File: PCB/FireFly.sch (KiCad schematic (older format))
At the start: 86 parts, among them Q1 LED_RGB 5050, Q2 MMBT2222, SW4 SWITCH

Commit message: Sch seems done
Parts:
- removed C2, C3: 0.1u, Capacitors:CAP_0603, symbol Tittar_kl:C
- removed C6: 1u, Capacitors:CAP_0603, symbol Tittar_kl:C
- removed C9: 10u, Capacitors:CAP_0603, symbol Tittar_kl:C
- removed L2: BLM15AG102SN1, Inductors:IND_0402, symbol Tittar_kl:L
- added C15: 100pF, Capacitors:CAP_0402, symbol Tittar_kl:C
- added C34: *, Capacitors:CAP_0402, symbol Tittar_kl:C
- added SW1, SW3: BUTTON, symbol Switches:BUTTON
- added XL2: CONN_5, symbol Connectors_kl:CONN_5
- C33: renamed from C23; value 3.3pF -> *
- C4: value 0.1u -> 12pF; footprint Capacitors:CAP_0603 -> Capacitors:CAP_0402; Price (none) -> 0.5; SolderPoints (none) -> 2
- C5: value 10n -> 12pF; footprint Capacitors:CAP_0603 -> Capacitors:CAP_0402; Price (none) -> 0.5; SolderPoints (none) -> 2
- L8: renamed from L4; value 8.2nH -> *
- gave numbers to parts that had none: 27
- renumbered ANT1 to ANT2, C10 to C18, C7 to C2, C11 to C22, C12 to C23, C13 to C24, C22 to C25, C14 to C26, C15 to C27, C16 to C28, C17 to C29, C18 to C30, C19 to C31, C26 to C32, C8 to C6, L3 to L7, R9 to R10, R12 to R11, R8 to R12, R1 to R2, R2 to R3, R3 to R4, R4 to R5, R5 to R7, R6 to R8, R7 to R9, SW4 to SW2, TP2 to TP1, TP3 to TP2, XL2 to XL3, XTAL1 to XTAL3
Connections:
- net labels added: P27, P28, P29
- net labels removed: ANT1, ANT2, BTN3, DIP1, DIP2, DIP3, DIP4, DIP5, DIP6, DIP7, DIP8, MCU_RX_NRF_TX, MCU_TX_NRF_RX, PwrMCU, SWCLK, SWDIO, UART_RX, UART_TX, Vibro_CTRL
- wire segments 327 -> 308
- no-connect marks 9 -> 4
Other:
- note added: "Just pins"
- note removed: "MCU Power Filter"
- note removed: "Pins 24, 36, 48, 1+9"
- moved on the sheet: ANT1, ANT2, B1, BLN1, BZ1, C1, C10, C11, C12, C13, C14, C16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

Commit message: pcb under construction
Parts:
- ANT1: footprint (none) -> Antennas:LcktSnd_868
- ANT2: footprint Antennas:Locket5 -> Antennas:LcktSnd_2d41
- DD1: footprint (none) -> SO_DIL_TSSOP:SO8_150MIL
- SW1, SW3: footprint (none) -> BtnsSwitches:BTN_4x4_SMD
- XL1: footprint (none) -> Connectors:PLD-8
- XL2: footprint (none) -> Connectors:PLS-5
- XTAL2: footprint CRYSTAL -> Quartz:03225C4
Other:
- moved on the sheet: Logo1
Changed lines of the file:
@@
 L pcb_details:Logo Logo1
 U 1 1 57188192
-P 14700 9150
-F 0 "Logo1" H 14600 9600 60  0000 C CNN
-F 1 "Logo" H 14900 9600 60  0000 C CNN
-F 2 "Pictures:Ostranna_12d7_10d1" H 14700 9150 60  0001 C CNN
-F 3 "" H 14700 9150 60  0000 C CNN
-	1    14700 9150
+P 15200 9150
+F 0 "Logo1" H 15100 9600 60  0000 C CNN
+F 1 "Logo" H 15400 9600 60  0000 C CNN
+F 2 "Pictures:Ostranna_12d7_10d1" H 15200 9150 60  0001 C CNN
+F 3 "" H 15200 9150 60  0000 C CNN
+	1    15200 9150
 	1    0    0    -1
 $EndComp
@@
 F 0 "XTAL2" V 6200 2650 50  0000 L CNN
 F 1 "32MHz" V 5950 2600 50  0000 L CNN
-F 2 "CRYSTAL" H 6125 3025 39  0001 C CNN
+F 2 "Quartz:03225C4" H 6125 3025 39  0001 C CNN
 F 3 "" H 6100 3175 60  0001 C CNN
 F 4 "15" H 6200 3275 60  0001 C CNN "Price"
@@
 F 0 "ANT1" H 8267 1647 60  0000 C CNN
 F 1 "ANT_GENERAL" H 8267 1541 60  0000 C CNN
-F 2 "" H 8400 1350 60  0000 C CNN
+F 2 "Antennas:LcktSnd_868" H 8400 1350 60  0001 C CNN
 F 3 "" H 8400 1350 60  0000 C CNN
 	1    8400 1350
@@
 F 0 "DD1" H 1450 4637 60  0000 C CNN
 F 1 "EEPROM_I2C" H 1450 4531 60  0000 C CNN
-F 2 "" H 2000 4400 60  0001 C CNN
+F 2 "SO_DIL_TSSOP:SO8_150MIL" H 2000 4400 60  0001 C CNN
 F 3 "" H 1900 4500 60  0001 C CNN
 F 4 "8" H 1600 4700 60  0001 C CNN "SolderPoints"
@@
 F 0 "XL1" H 842 2036 50  0000 C CNN
 F 1 "CONN_8" H 842 1945 50  0000 C CNN
-F 2 "" H 900 1450 60  0000 C CNN
+F 2 "Connectors:PLD-8" H 900 1450 60  0001 C CNN
 F 3 "" H 900 1450 60  0000 C CNN
 	1    900  1450
@@
 F 0 "ANT2" H 15150 1550 60  0000 C CNN
 F 1 "ANT_PCB_MONO_2PIN" H 15400 1550 60  0001 C CNN
-F 2 "Antennas:Locket5" H 15050 1400 60  0001 C CNN
+F 2 "Antennas:LcktSnd_2d41" H 15050 1400 60  0001 C CNN
 F 3 "" H 15050 1400 60  0000 C CNN
 F 4 "0" H 15050 1400 60  0001 C CNN "Price"
@@
 F 0 "SW1" H 6150 8605 50  0000 C CNN
 F 1 "BUTTON" H 6150 8514 50  0000 C CNN
-F 2 "" H 6150 8350 60  0000 C CNN
+F 2 "BtnsSwitches:BTN_4x4_SMD" H 6150 8350 60  0001 C CNN
 F 3 "" H 6150 8350 60  0000 C CNN
 	1    6150 8350
@@
 F 0 "SW3" H 7650 8605 50  0000 C CNN
 F 1 "BUTTON" H 7650 8514 50  0000 C CNN
-F 2 "" H 7650 8350 60  0000 C CNN
+F 2 "BtnsSwitches:BTN_4x4_SMD" H 7650 8350 60  0001 C CNN
 F 3 "" H 7650 8350 60  0000 C CNN
 	1    7650 8350
@@
 F 0 "XL2" H 842 3186 50  0000 C CNN
 F 1 "CONN_5" H 842 3095 50  0000 C CNN
-F 2 "" H 900 2750 60  0000 C CNN
+F 2 "Connectors:PLS-5" H 900 2750 60  0001 C CNN
 F 3 "" H 900 2750 60  0000 C CNN
 	1    900  2750

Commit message: v1 sent to factory
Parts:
- removed C15, C32: 100pF, Capacitors:CAP_0402, symbol Tittar_kl:C
- removed C16, C20: *, Capacitors:CAP_0402, symbol Tittar_kl:C
- removed L5: *, Inductors:IND_0402, symbol Tittar_kl:L
- removed RP3, RP4: REFPOINT, PCB:REF_POINT_1MM, symbol pcb_details:REFPOINT
- removed XL2: CONN_5, Connectors:PLS-5, symbol Connectors_kl:CONN_5
- added XL2: CONN_4, Connectors:PLS-4, symbol Connectors_kl:CONN_4
- ANT1: footprint Antennas:LcktSnd_868 -> Antennas:Firefly_2400; symbol Antennas_kl:ANT_GENERAL -> Antennas_kl:ANT_PCB_MONO
- ANT2: footprint Antennas:LcktSnd_2d41 -> Antennas:Firefly_868; symbol Antennas_kl:ANT_PCB_MONO_2PIN -> Antennas_kl:ANT_PCB_MONO
- C14, C17, C2, C21, C22, C23, C24, C26, C27, C28, C29, C3, C30, C31, C9: footprint Capacitors:CAP_0603 -> Capacitors:CAP_0402
- XL1: footprint Connectors:PLD-8 -> Connectors:PLD-8_LOCK
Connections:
- net P29 is gone; now on net VDD_NRF: DD2.41 (P0.29/AIN5)
- net +BATT: now also XL2.2 (PM)
- net GND: now also XL2.1 (P1); no longer ANT1.2 (GND), ANT2.2
- net NRF_NRST: now also XL1.8; no longer XL1.7
- net NRF_SWCLK: now also XL1.4; no longer XL1.2
- net NRF_SWDIO: now also XL1.2; no longer XL1.4
- net NRF_SWO: now also XL1.7; no longer XL1.8
- net P27: now also XL2.3
- net P28: now also XL2.4
- net RF3: now also C33.1, L8.2
- net RF2400: now reaches ANT1.1
- net RF2400: now also L3.2
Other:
- note added: "Battery\nmeasurement"
- moved on the sheet: C33, C34, L8

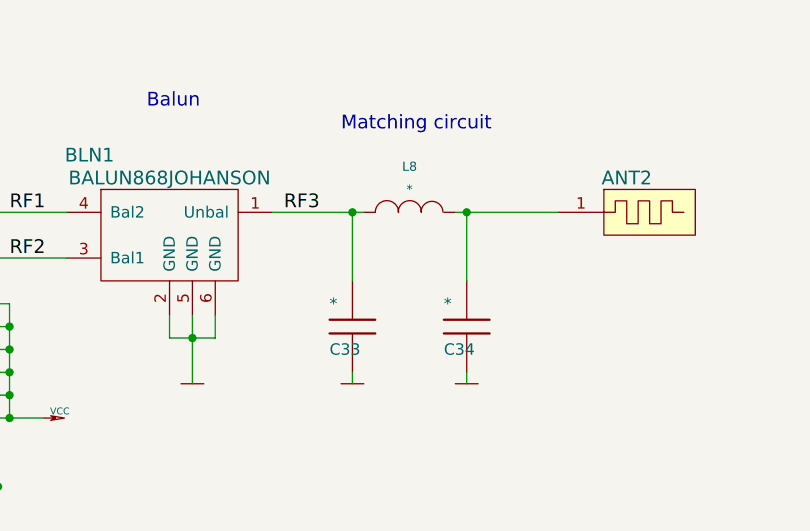
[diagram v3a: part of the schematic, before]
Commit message: Antenna matched
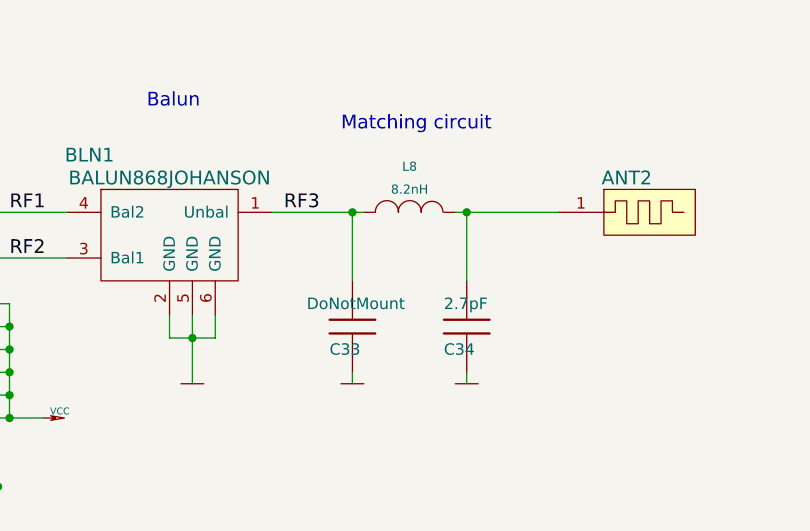
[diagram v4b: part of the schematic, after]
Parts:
- C33: value * -> DoNotMount
- C34: value * -> 2.7pF
- L8: value * -> 8.2nH
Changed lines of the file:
@@
 EESchema Schematic File Version 5
 LIBS:FireFly-cache
-EELAYER 29 0
+EELAYER 30 0
 EELAYER END
 $Descr A3 16535 11693
@@
 Comment3 ""
 Comment4 ""
+Comment5 ""
+Comment6 ""
+Comment7 ""
+Comment8 ""
+Comment9 ""
 $EndDescr
 $Comp
@@
 P 13550 1850
 F 0 "C33" H 13450 1750 50  0000 L CNN
-F 1 "*" H 13450 1950 50  0000 L CNN
+F 1 "DoNotMount" H 13350 1950 50  0000 L CNN
 F 2 "Capacitors:CAP_0402" V 13650 1700 28  0001 C BNN
 F 3 "" H 13450 1750 60  0001 C CNN
@@
 P 14050 1850
 F 0 "C34" H 13950 1750 50  0000 L CNN
-F 1 "*" H 13950 1950 50  0000 L CNN
+F 1 "2.7pF" H 13950 1950 50  0000 L CNN
 F 2 "Capacitors:CAP_0402" V 14150 1700 28  0001 C BNN
 F 3 "" H 13950 1750 60  0001 C CNN
@@
 P 13800 1350
 F 0 "L8" V 14000 1350 40  0000 C CNN
-F 1 "*" V 13900 1350 40  0000 C CNN
+F 1 "8.2nH" V 13900 1350 40  0000 C CNN
 F 2 "Inductors:IND_0402" V 13860 1360 40  0001 C CNN
 F 3 "" V 13700 1210 60  0001 C CNN

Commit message: Preparing for production
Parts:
- added D2: BAT54WS, Diodes:SOD323, symbol Tittar_kl:D_Shottky
- B1: footprint Installation:BATTERY_AAA_X2 -> Installation:BATTERY_AAA_X2_PLUS_LEFT
- BZ1: value PS-9627 -> KLJ-09650-3027; footprint Installation:BUZZER_HC0903 -> Installation:BUZZER_KLJ-09650-3027; Price 10 -> (none); URL http://www.quartz1.com/price/model.php?akt=7940.06 -> (none)
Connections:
- net +BATT: now also D2.C
- net BuzzerOut: now also D2.A
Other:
- moved on the sheet: BZ1
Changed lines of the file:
@@
 EESchema Schematic File Version 5
-LIBS:FireFly-cache
 EELAYER 30 0
 EELAYER END
@@
 $EndComp
 Wire Wire Line
-	7700 6250 7950 6250
+	7800 6250 7850 6250
 Wire Wire Line
 	5200 6450 5650 6450
@@
 	6150 6450 6250 6450
 Wire Wire Line
-	6500 6250 7200 6250
+	6500 6250 7250 6250
 $Comp
 L Transistors_kl:NPN Q2
@@
 L power:+BATT #PWR042
 U 1 1 572478CD
-P 7950 6250
-F 0 "#PWR042" H 7950 6210 30  0001 C CNN
-F 1 "+BATT" H 8030 6280 30  0000 C CNN
-F 2 "" H 7950 6250 60  0000 C CNN
-F 3 "" H 7950 6250 60  0000 C CNN
-	1    7950 6250
+P 8050 6250
+F 0 "#PWR042" H 8050 6210 30  0001 C CNN
+F 1 "+BATT" H 8130 6280 30  0000 C CNN
+F 2 "" H 8050 6250 60  0000 C CNN
+F 3 "" H 8050 6250 60  0000 C CNN
+	1    8050 6250
 	1    0    0    -1
 $EndComp
@@
 L Tittar_kl:BUZZER BZ1
 U 1 1 57C421AE
-P 7450 6250
-F 0 "BZ1" V 7150 6350 60  0000 C CNN
-F 1 "PS-9627" V 7300 6250 60  0000 C CNN
-F 2 "Installation:BUZZER_HC0903" H 7450 6250 60  0001 C CNN
-F 3 "" H 7450 6250 60  0000 C CNN
-F 4 "http://www.quartz1.com/price/model.php?akt=7940.06" H 7450 6250 60  0001 C CNN "URL"
-F 5 "10" H 7450 6250 60  0001 C CNN "Price"
-	1    7450 6250
+P 7550 6250
+F 0 "BZ1" V 7250 6350 60  0000 C CNN
+F 1 "KLJ-09650-3027" V 7400 6250 60  0000 C CNN
+F 2 "Installation:BUZZER_KLJ-09650-3027" H 7550 6250 60  0001 C CNN
+F 3 "" H 7550 6250 60  0000 C CNN
+F 4 "" H 7550 6250 60  0001 C CNN "URL"
+F 5 "" H 7550 6250 60  0001 C CNN "Price"
+	1    7550 6250
 	0    -1   1    0
 $EndComp
@@
 F 0 "B1" H 6100 10600 60  0000 C CNN
 F 1 "BAT_HOLDER" H 6300 10650 60  0001 C CNN
-F 2 "Installation:BATTERY_AAA_X2" H 6000 10500 60  0001 C CNN
+F 2 "Installation:BATTERY_AAA_X2_PLUS_LEFT" H 6000 10500 60  0001 C CNN
 F 3 "" H 6000 10500 60  0000 C CNN
 F 4 "5" H 6000 10500 60  0001 C CNN "Price"
@@
 Text Label 6800 1300 0    50   ~ 0
 RF2400
+$Comp
+L Tittar_kl:D_Shottky D2
+U 1 1 5DF935EC
+P 7550 6500
+F 0 "D2" H 7400 6600 40  0000 C CNN
+F 1 "BAT54WS" H 7650 6600 40  0000 C CNN
+F 2 "Diodes:SOD323" H 7550 6500 60  0001 C CNN
+F 3 "" H 7550 6500 60  0000 C CNN
+F 4 "https://www.terraelectronica.ru/catalog_info.php?CODE=182655" H 7550 6500 60  0001 C CNN "URL"
+F 5 "2.5" H 7550 6500 60  0001 C CNN "Price"
+F 6 "2" H 7550 6500 60  0001 C CNN "SolderPoints"
+	1    7550 6500
+	1    0    0    -1
+$EndComp
+Wire Wire Line
+	7400 6500 7250 6500
+Wire Wire Line
+	7250 6500 7250 6250
+Connection ~ 7250 6250
+Wire Wire Line
+	7250 6250 7300 6250
+Wire Wire Line
+	7700 6500 7850 6500
+Wire Wire Line
+	7850 6500 7850 6250
+Connection ~ 7850 6250
+Wire Wire Line
+	7850 6250 8050 6250
 $EndSCHEMATC
